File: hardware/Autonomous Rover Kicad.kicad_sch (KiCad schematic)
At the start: 6 parts, among them J1 MPU6050, J2 Arducam OV2640, J3 ESP32-S3, J4 9V Battery Input, J5 L298N Logic, J6 L298N Power

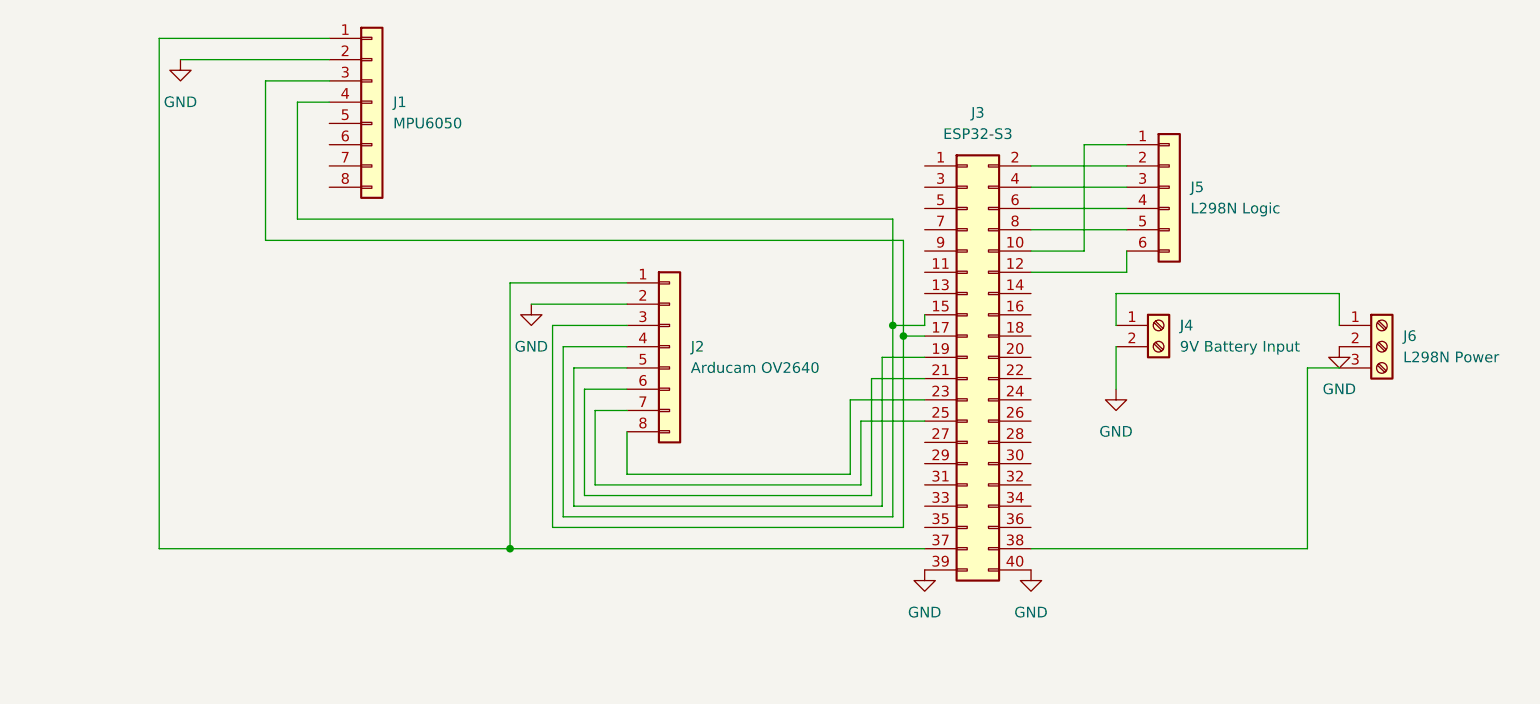
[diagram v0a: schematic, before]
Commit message: Clean up schematic: ERC 0, net labels, decoupling caps
KiCad ERC now passes with 0 violations (was 29 - all unannotated unused pins
plus a missing power flag), verified with kicad-cli 9.0.

- Add no-connect flags to the 28 intentionally-unused module pins (MPU6050
  J1.5-8 and the unused ESP32/J3 GPIOs).
- Add a PWR_FLAG on GND so ERC knows the rail is externally powered.
- Name the nets: +5V, +3V3, VMOTOR, I2C_SDA, I2C_SCL, CAM_SPI1-4,
  MOT_CTRL1-6 (were auto-named Net-Jx-Pin_y).
- Add bulk decoupling: C1 100uF on +5V, C2 470uF on VMOTOR, C3 10uF on +3V3
  to harden against motor-transient brownouts (the same risk the firmware
  PWM duty cap guards against). Connectivity confirmed via netlist export.

Note: only the schematic changed; the PCB and Gerbers are untouched. The three
capacitors are captured as design intent - run Update-PCB-from-Schematic in
KiCad, place and route them, then re-plot the Gerbers to add them to the board.

Co-Authored-By: Claude Opus 4.8 <noreply@anthropic.com>
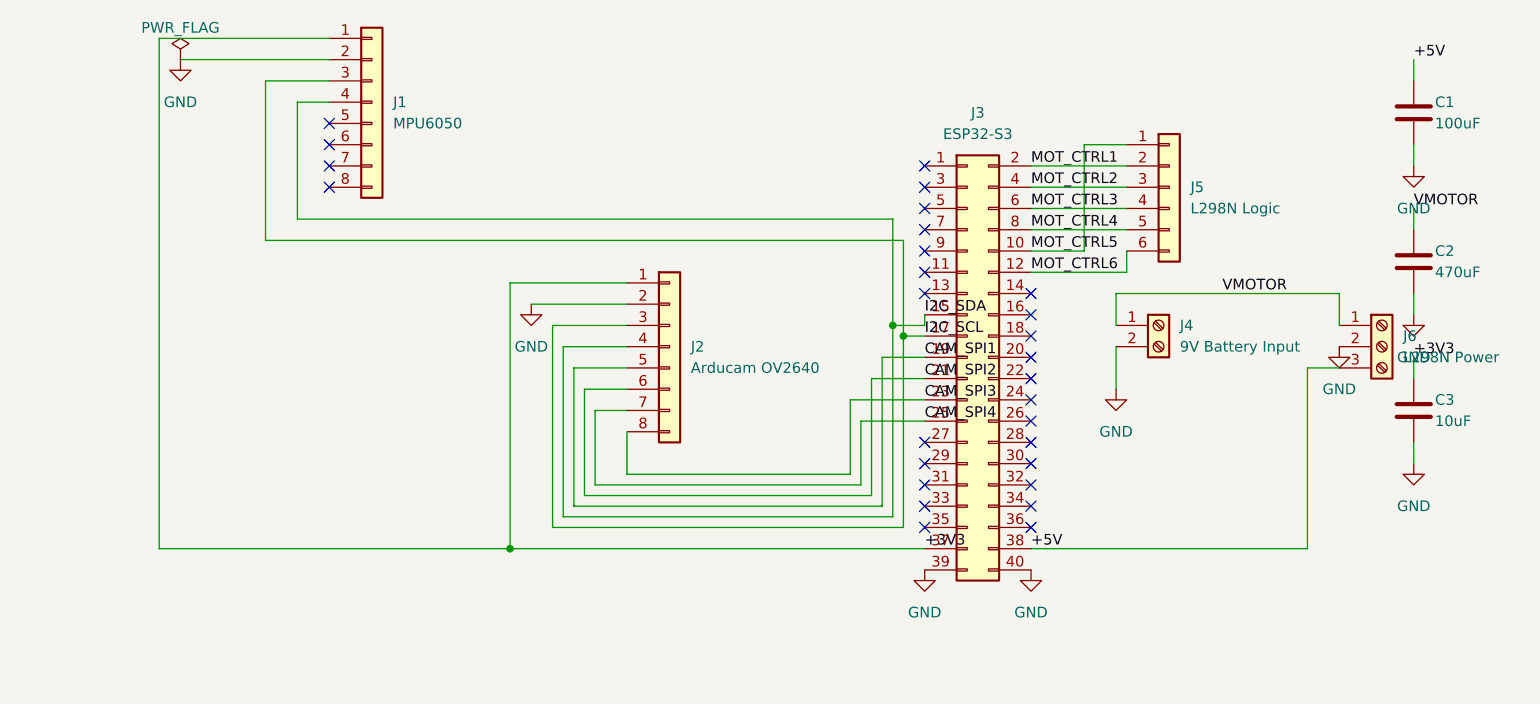
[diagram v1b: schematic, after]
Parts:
- added C1: 100uF, symbol Device:C
- added C2: 470uF, symbol Device:C
- added C3: 10uF, symbol Device:C
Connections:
- net GND: now also C1.2, C2.2, C3.2
- net MOT_CTRL5: now reaches J3.10 (Pin_10), J5.1 (Pin_1)
- net MOT_CTRL1: now reaches J3.2 (Pin_2), J5.2 (Pin_2)
- net MOT_CTRL2: now reaches J3.4 (Pin_4), J5.3 (Pin_3)
- net MOT_CTRL3: now reaches J3.6 (Pin_6), J5.4 (Pin_4)
- net MOT_CTRL4: now reaches J3.8 (Pin_8), J5.5 (Pin_5)
- net MOT_CTRL6: now reaches J3.12 (Pin_12), J5.6 (Pin_6)
- net VMOTOR: now reaches J4.1 (Pin_1), J6.1 (Pin_1)
- net VMOTOR: now also C2.1
- net +5V: now reaches J3.38 (Pin_38), J6.3 (Pin_3)
- net +5V: now also C1.1
- net +3V3: now reaches J1.1 (Pin_1), J2.1 (Pin_1), J3.37 (Pin_37)
- net +3V3: now also C3.1
- net I2C_SCL: now reaches J1.3 (Pin_3), J2.3 (Pin_3), J3.17 (Pin_17)
- net I2C_SDA: now reaches J1.4 (Pin_4), J2.4 (Pin_4), J3.15 (Pin_15)
- net CAM_SPI1: now reaches J2.5 (Pin_5), J3.19 (Pin_19)
- net CAM_SPI2: now reaches J2.6 (Pin_6), J3.21 (Pin_21)
- net CAM_SPI4: now reaches J2.7 (Pin_7), J3.25 (Pin_25)
- net CAM_SPI3: now reaches J2.8 (Pin_8), J3.23 (Pin_23)
- no-connect marks 0 -> 28

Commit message: Caps: use polarized C_Polarized symbol + assign THT footprints
- C1 100uF (+5V)    -> Capacitor_THT:CP_Radial_D6.3mm_P2.50mm
- C2 470uF (VMOTOR) -> Capacitor_THT:CP_Radial_D8.0mm_P3.50mm
- C3 10uF  (+3V3)   -> Capacitor_THT:CP_Radial_D5.0mm_P2.50mm

Pin 1 (+) stays on the rail, pin 2 (-) on GND. Verified with kicad-cli: ERC 0,
netlist confirms the polarized symbol and footprints. The large line diff is
mostly KiCad re-save formatting from the prior editing session.

Co-Authored-By: Claude Opus 4.8 <noreply@anthropic.com>
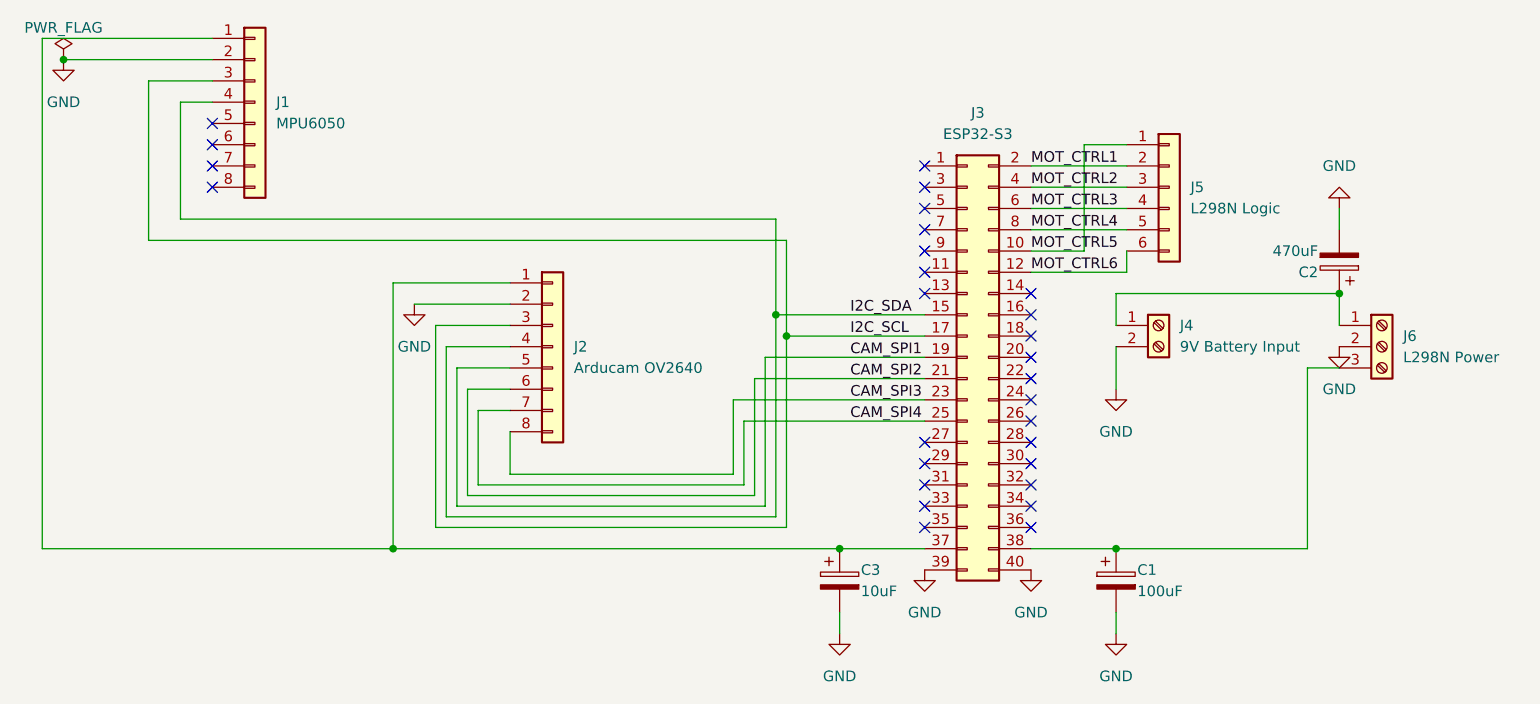
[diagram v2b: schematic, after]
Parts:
- C1: footprint (none) -> Capacitor_THT:CP_Radial_D6.3mm_P2.50mm; symbol Device:C -> Device:C_Polarized
- C2: footprint (none) -> Capacitor_THT:CP_Radial_D8.0mm_P3.50mm; symbol Device:C -> Device:C_Polarized
- C3: footprint (none) -> Capacitor_THT:CP_Radial_D5.0mm_P2.50mm; symbol Device:C -> Device:C_Polarized
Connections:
- net +3V3: no longer names the net of C3.1, J1.1 (Pin_1), J2.1 (Pin_1), J3.37 (Pin_37)
- net +5V: no longer names the net of C1.1, J3.38 (Pin_38), J6.3 (Pin_3)
- net VMOTOR: no longer names the net of C2.1, J4.1 (Pin_1), J6.1 (Pin_1)
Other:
- moved on the sheet: J1, J2
